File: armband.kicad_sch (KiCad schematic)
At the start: 14 parts, among them IC1 QSMP-1570, SW1 EVP-BB2A9B000, SW2 EVP-BB2A9B000

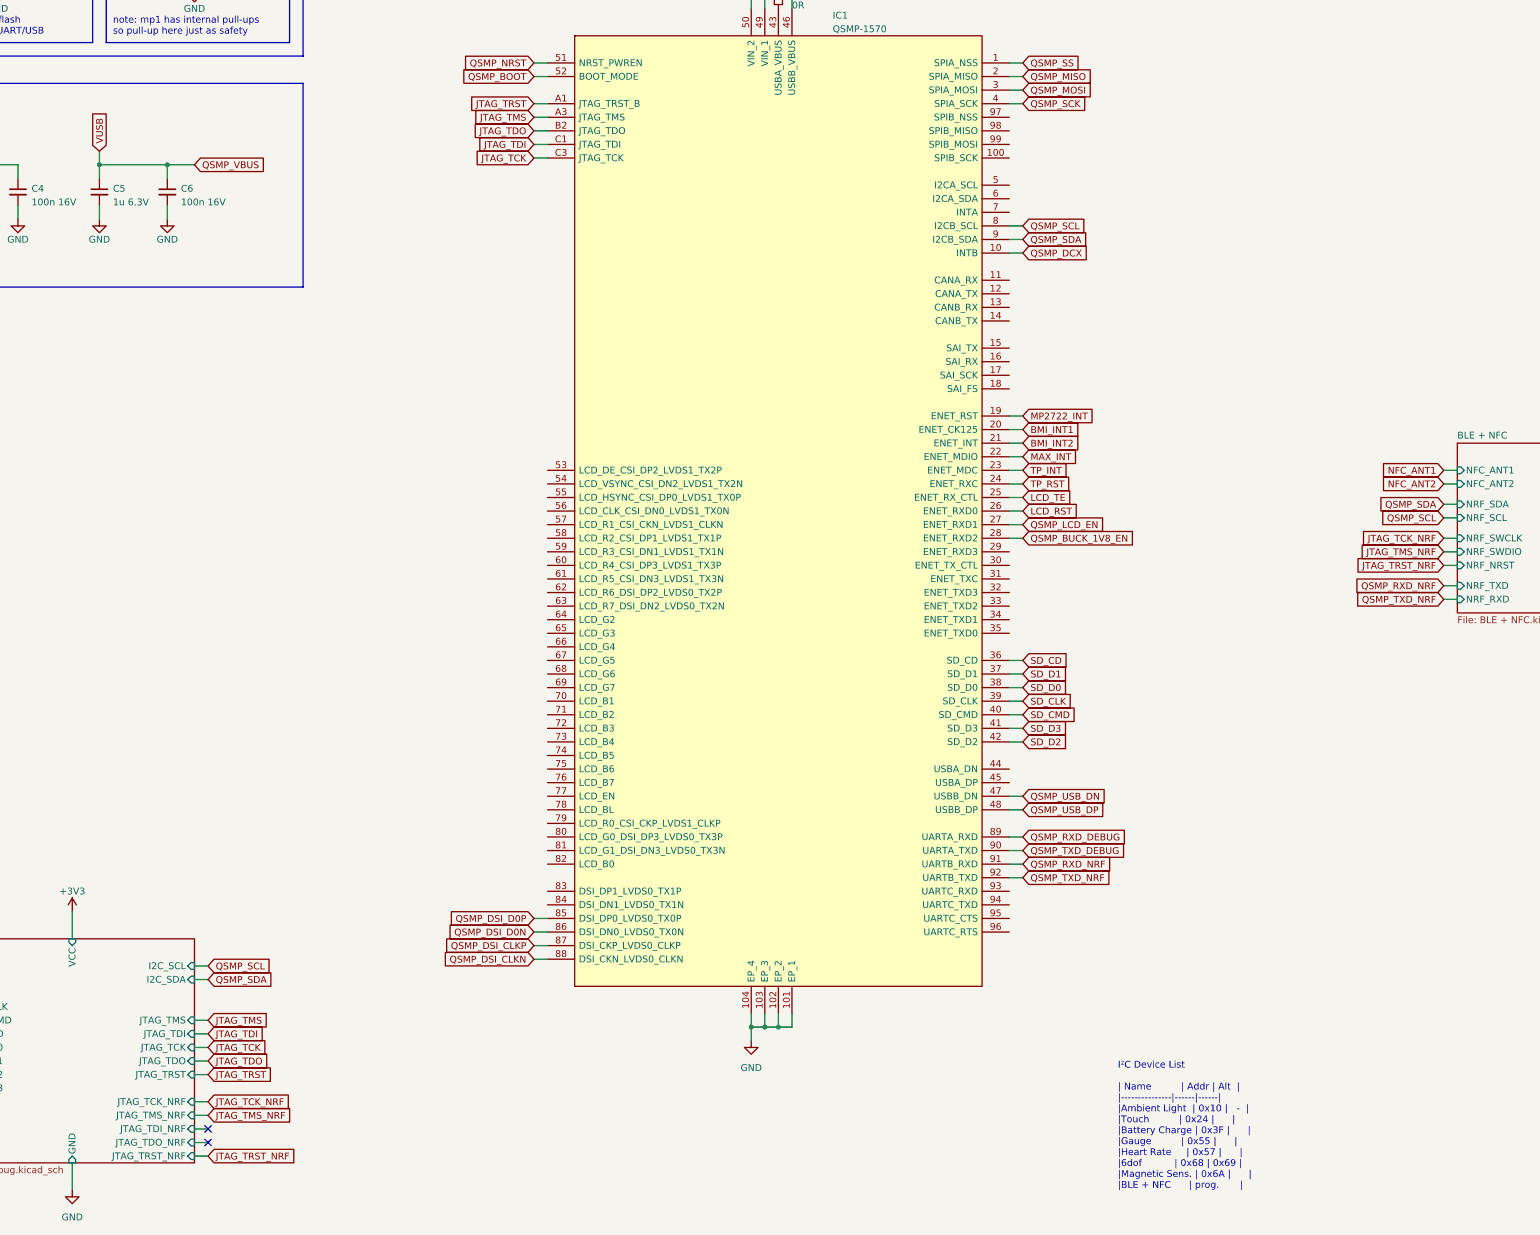
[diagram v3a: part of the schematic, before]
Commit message: updated schematic
- renamed JTAG (QSMP) and SWD (NRF) labels
- added footprint to misc. connector in debug.kicad_sch
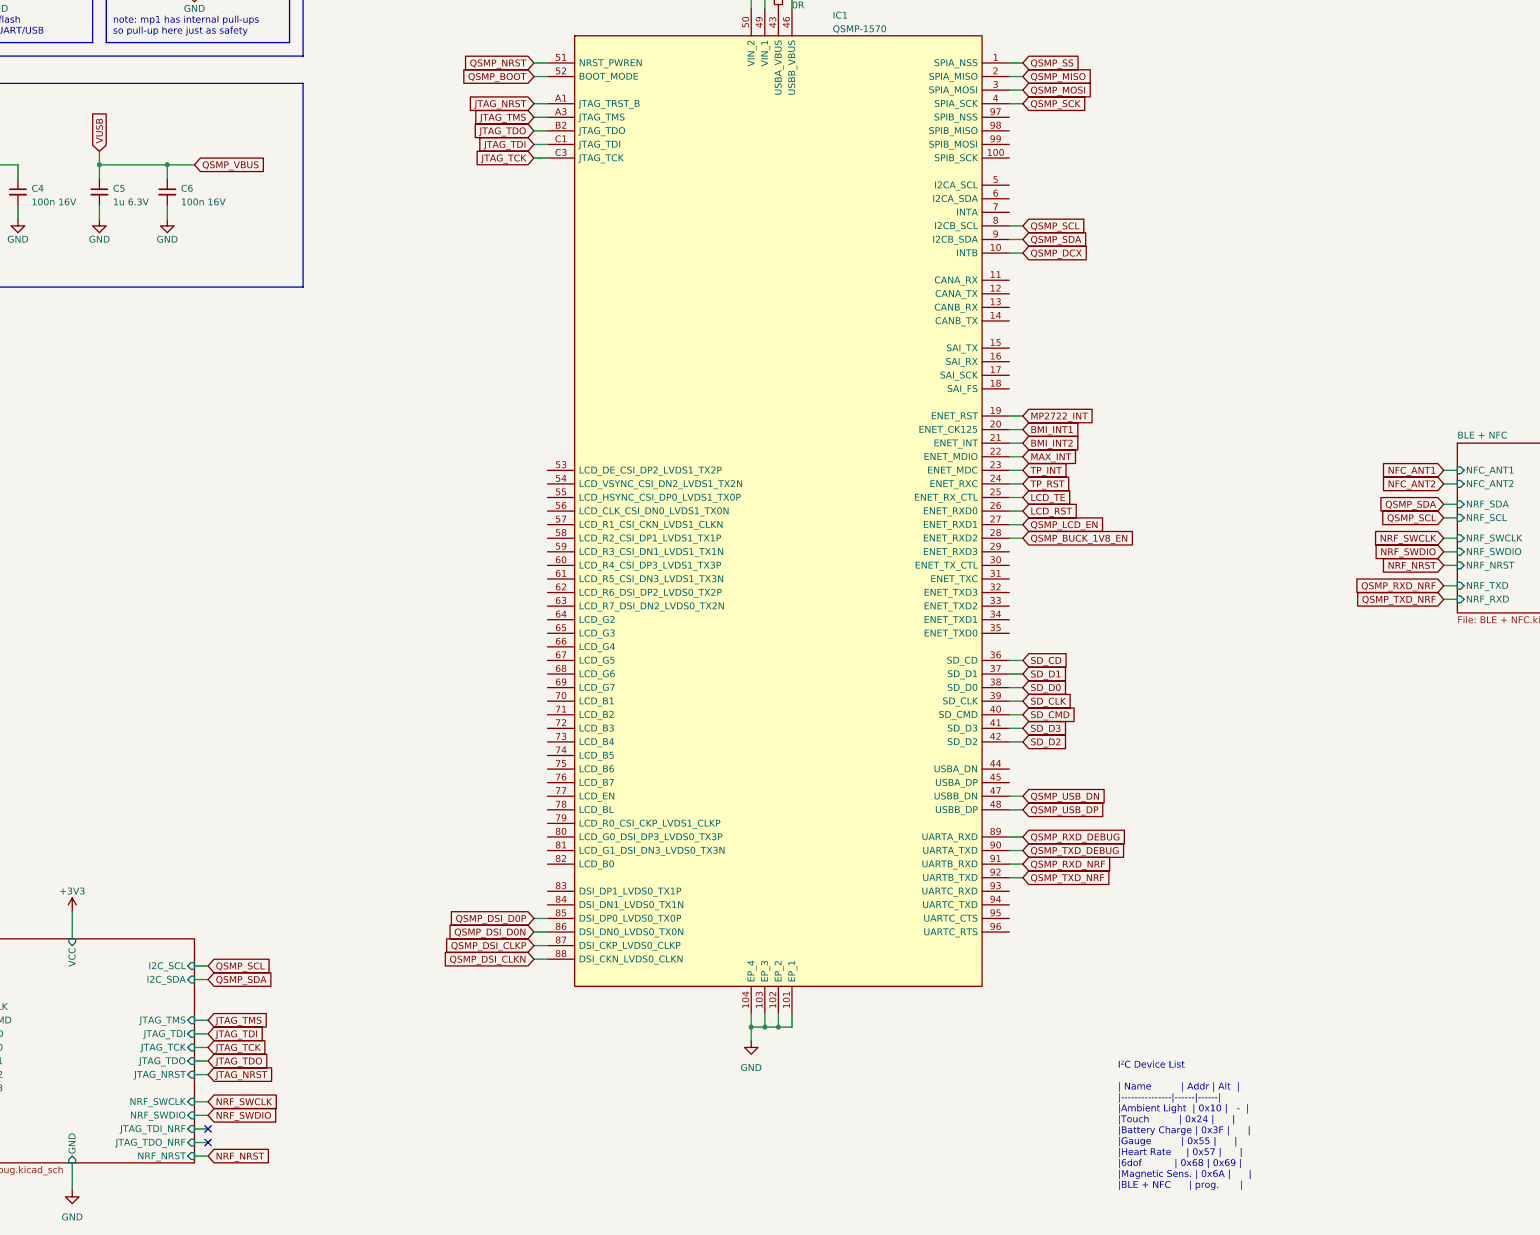
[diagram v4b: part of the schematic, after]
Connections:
- net JTAG_TRST renamed JTAG_NRST
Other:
- sheet debug ports: added JTAG_NRST, NRF_NRST, NRF_SWCLK, NRF_SWDIO; removed JTAG_TCK_NRF, JTAG_TMS_NRF, JTAG_TRST, JTAG_TRST_NRF
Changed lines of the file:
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@@
     )
   )
-  (global_label "JTAG_TMS_NRF" (shape input) (at 83.82 265.43 0) (fields_autoplaced)
+  (global_label "NRF_SWDIO" (shape input) (at 83.82 265.43 0) (fields_autoplaced)
     (effects (font (size 1.27 1.27)) (justify left))
     (property "Intersheetrefs" "${INTERSHEET_REFS}" (at 100.3518 265.43 0)
@@
     )
   )
-  (global_label "JTAG_TRST_NRF" (shape input) (at 314.96 162.56 180) (fields_autoplaced)
+  (global_label "NRF_NRST" (shape input) (at 314.96 162.56 180) (fields_autoplaced)
     (effects (font (size 1.27 1.27)) (justify right))
     (property "Intersheetrefs" "${INTERSHEET_REFS}" (at 297.642 162.56 0)
@@
     )
   )
-  (global_label "JTAG_TRST" (shape input) (at 144.78 76.2 180) (fields_autoplaced)
+  (global_label "JTAG_NRST" (shape input) (at 144.78 76.2 180) (fields_autoplaced)
     (effects (font (size 1.27 1.27)) (justify right))
     (property "Intersheetrefs" "${INTERSHEET_REFS}" (at 88.9 -25.4 0)
@@
     )
   )
-  (global_label "JTAG_TCK_NRF" (shape input) (at 314.96 157.48 180) (fields_autoplaced)
+  (global_label "NRF_SWCLK" (shape input) (at 314.96 157.48 180) (fields_autoplaced)
     (effects (font (size 1.27 1.27)) (justify right))
     (property "Intersheetrefs" "${INTERSHEET_REFS}" (at 298.5491 157.48 0)
@@
     )
   )
-  (global_label "JTAG_TMS_NRF" (shape input) (at 314.96 160.02 180) (fields_autoplaced)
+  (global_label "NRF_SWDIO" (shape input) (at 314.96 160.02 180) (fields_autoplaced)
     (effects (font (size 1.27 1.27)) (justify right))
     (property "Intersheetrefs" "${INTERSHEET_REFS}" (at 298.4282 160.02 0)
@@
     )
   )
-  (global_label "JTAG_TCK_NRF" (shape input) (at 83.82 262.89 0) (fields_autoplaced)
+  (global_label "NRF_SWCLK" (shape input) (at 83.82 262.89 0) (fields_autoplaced)
     (effects (font (size 1.27 1.27)) (justify left))
     (property "Intersheetrefs" "${INTERSHEET_REFS}" (at 100.2309 262.89 0)
@@
     )
   )
-  (global_label "JTAG_TRST_NRF" (shape input) (at 83.82 273.05 0) (fields_autoplaced)
+  (global_label "NRF_NRST" (shape input) (at 83.82 273.05 0) (fields_autoplaced)
     (effects (font (size 1.27 1.27)) (justify left))
     (property "Intersheetrefs" "${INTERSHEET_REFS}" (at 101.138 273.05 0)
@@
     )
   )
-  (global_label "JTAG_TRST" (shape input) (at 83.82 257.81 0) (fields_autoplaced)
+  (global_label "JTAG_NRST" (shape input) (at 83.82 257.81 0) (fields_autoplaced)
     (effects (font (size 1.27 1.27)) (justify left))
     (property "Intersheetrefs" "${INTERSHEET_REFS}" (at 137.16 151.13 0)
@@
       (effects (font (size 1.27 1.27)) (justify right))
     )
-    (pin "JTAG_TRST" input (at 81.28 257.81 0)
+    (pin "JTAG_NRST" input (at 81.28 257.81 0)
       (effects (font (size 1.27 1.27)) (justify right))
     )
@@
       (effects (font (size 1.27 1.27)) (justify left))
     )
-    (pin "JTAG_TCK_NRF" input (at 81.28 262.89 0)
-      (effects (font (size 1.27 1.27)) (justify right))
-    )
-    (pin "JTAG_TMS_NRF" input (at 81.28 265.43 0)
+    (pin "NRF_SWCLK" input (at 81.28 262.89 0)
+      (effects (font (size 1.27 1.27)) (justify right))
+    )
+    (pin "NRF_SWDIO" input (at 81.28 265.43 0)
       (effects (font (size 1.27 1.27)) (justify right))
     )
@@
       (effects (font (size 1.27 1.27)) (justify right))
     )
-    (pin "JTAG_TRST_NRF" input (at 81.28 273.05 0)
-      (effects (font (size 1.27 1.27)) (justify right))
-    )
+    (pin "NRF_NRST" input (at 81.28 273.05 0)
+      (effects (font (size 1.27 1.27)) (justify right))
+    )

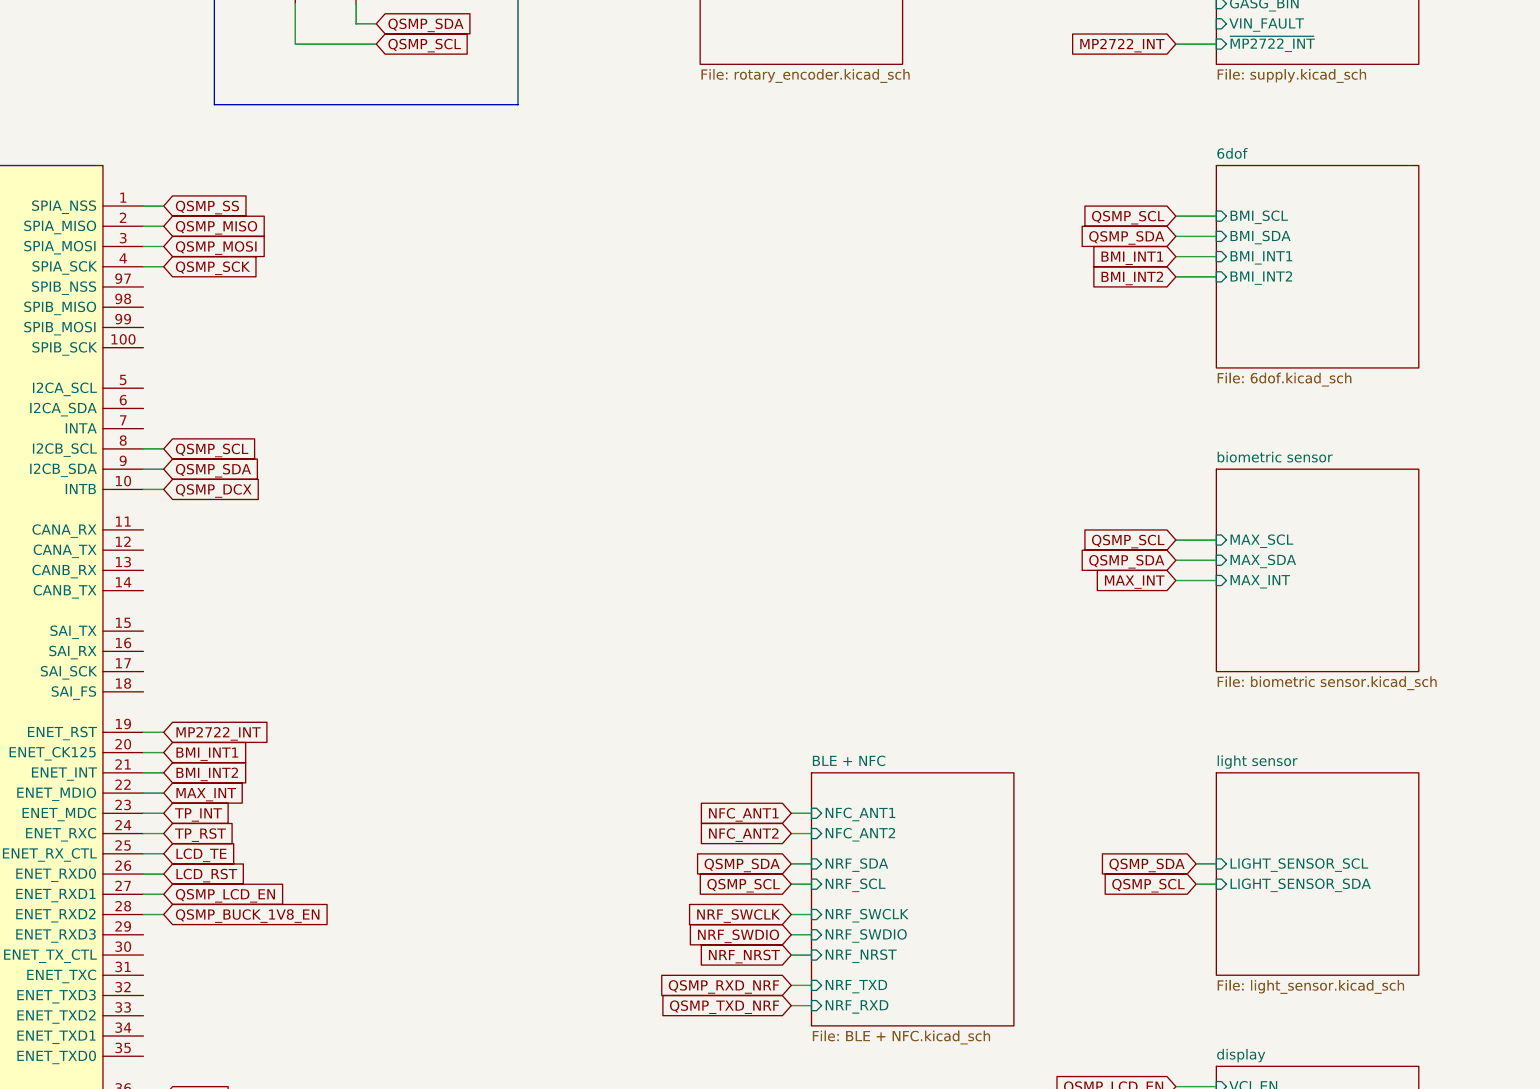
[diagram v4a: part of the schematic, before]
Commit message: added bmm350.kicad_mod and changed 9dof.kicad_sch
+ added symbol and footprint for magnetometer BMM350
+ changed supply of BMI (6dof) to 1v8
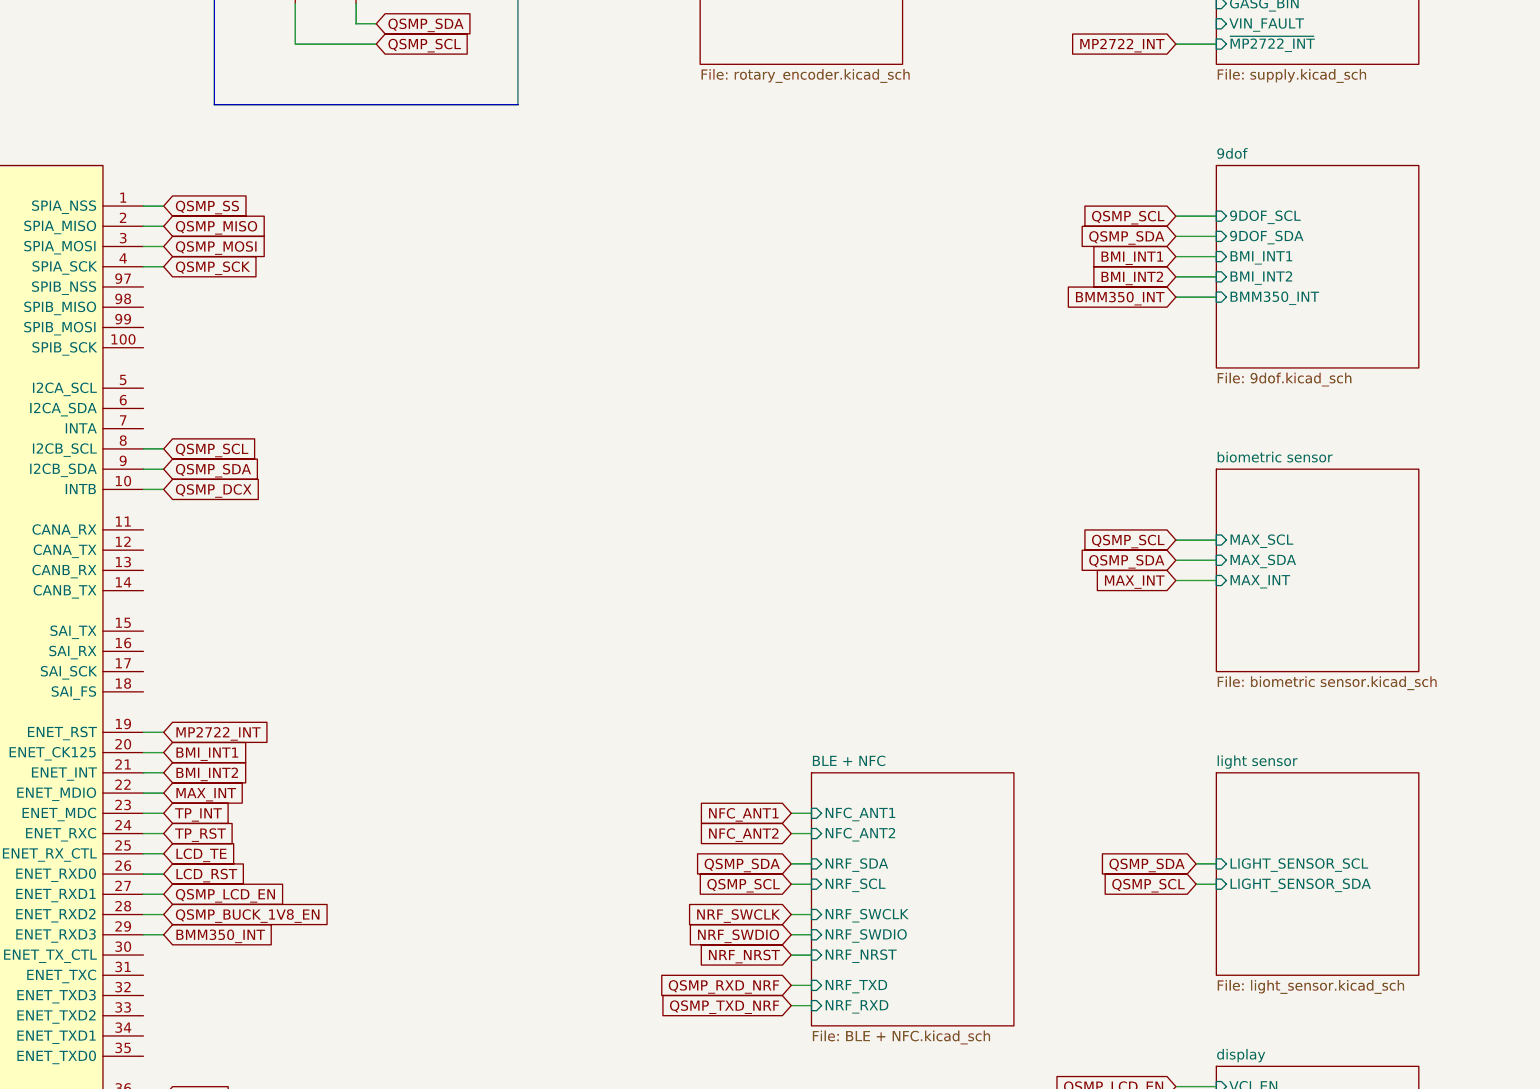
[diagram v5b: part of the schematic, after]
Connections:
- net BMM350_INT: now reaches IC1.29 (ENET_RXD3)
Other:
- sheet 6dof renamed 9dof
- sheet 9dof: file 6dof.kicad_sch -> 9dof.kicad_sch
- sheet 9dof ports: added 9DOF_SCL, 9DOF_SDA, BMM350_INT; removed BMI_SCL, BMI_SDA
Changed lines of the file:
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@@
+    (stroke (width 0) (type default))
+  )
+  (wire (pts (xy 233.68 160.02) (xy 236.22 160.02))
     (stroke (width 0) (type default))
   )
@@
   )
   (wire (pts (xy 233.68 76.2) (xy 236.22 76.2))
+    (stroke (width 0) (type default))
+  )
+  (wire (pts (xy 363.22 80.01) (xy 368.3 80.01))
     (stroke (width 0) (type default))
   )
@@
     )
   )
+  (global_label "BMM350_INT" (shape input) (at 236.22 160.02 0) (fields_autoplaced)
+    (effects (font (size 1.27 1.27)) (justify left))
+    (property "Intersheetrefs" "${INTERSHEET_REFS}" (at 250.7976 160.02 0)
+      (effects (font (size 1.27 1.27)) (justify left) hide)
+    )
+  )
   (global_label "JTAG_NRST" (shape input) (at 144.78 76.2 180) (fields_autoplaced)
     (effects (font (size 1.27 1.27)) (justify right))
@@
     (effects (font (size 1.27 1.27)) (justify right))
     (property "Intersheetrefs" "${INTERSHEET_REFS}" (at 346.2233 186.69 0)
+      (effects (font (size 1.27 1.27)) (justify right) hide)
+    )
+  )
+  (global_label "BMM350_INT" (shape input) (at 363.22 80.01 180) (fields_autoplaced)
+    (effects (font (size 1.27 1.27)) (justify right))
+    (property "Intersheetrefs" "${INTERSHEET_REFS}" (at 348.6424 80.01 0)
       (effects (font (size 1.27 1.27)) (justify right) hide)
     )
@@
     (stroke (width 0.1524) (type solid))
     (fill (color 0 0 0 0.0000))
-    (property "Sheetname" "6dof" (at 368.3 62.7884 0)
+    (property "Sheetname" "9dof" (at 368.3 62.7884 0)
       (effects (font (size 1.27 1.27)) (justify left bottom))
     )
-    (property "Sheetfile" "6dof.kicad_sch" (at 368.3 89.4846 0)
+    (property "Sheetfile" "9dof.kicad_sch" (at 368.3 89.4846 0)
       (effects (font (size 1.27 1.27)) (justify left top))
     )
-    (pin "BMI_SCL" input (at 368.3 69.85 180)
-      (effects (font (size 1.27 1.27)) (justify left))
-    )
-    (pin "BMI_SDA" input (at 368.3 72.39 180)
+    (pin "9DOF_SDA" input (at 368.3 72.39 180)
       (effects (font (size 1.27 1.27)) (justify left))
     )
@@
       (effects (font (size 1.27 1.27)) (justify left))
     )
+    (pin "9DOF_SCL" input (at 368.3 69.85 180)
+      (effects (font (size 1.27 1.27)) (justify left))
+    )
+    (pin "BMM350_INT" input (at 368.3 80.01 180)
+      (effects (font (size 1.27 1.27)) (justify left))
+    )

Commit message: Update 3d models
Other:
- note added: "I²C Device List | Name | Addr | Alt | |---------------|------|------| |Ambient Light | 0x10 | - | |BMM350 | 0x14 | 0x15 | |Touch | 0x24 | | |Battery Charge | 0x3F | | |Gauge | 0x55 | | |Heart Rate | 0x57 | | |6dof | 0x68 | 0x69 | |Magnetic Sens. | 0x6A | | |BLE + NFC | prog. |"
- note removed: "I²C Device List | Name | Addr | Alt | |---------------|------|------| |Ambient Light | 0x10 | - | |Touch | 0x24 | | |Battery Charge | 0x3F | | |Gauge | 0x55 | | |Heart Rate | 0x57 | | |6dof | 0x68 | 0x69 | |Magnetic Sens. | 0x6A | | |BLE + NFC | prog. |"
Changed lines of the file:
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@@
     (effects (font (size 1.27 1.27)) (justify left bottom))
   )
-  (text "I²C Device List\n\n| Name          | Addr | Alt  |\n|---------------|------|------|\n|Ambient Light  | 0x10 |   -  |\n|Touch          | 0x24 |      |\n|Battery Charge | 0x3F |      |  \n|Gauge          | 0x55 |      |  \n|Heart Rate     | 0x57 |      |\n|6dof           | 0x68 | 0x69 |\n|Magnetic Sens. | 0x6A |      |\n|BLE + NFC      | prog.       |"
+  (text "I²C Device List\n\n| Name          | Addr | Alt  |\n|---------------|------|------|\n|Ambient Light  | 0x10 |   -  |\n|BMM350         | 0x14 | 0x15 |\n|Touch          | 0x24 |      |\n|Battery Charge | 0x3F |      |  \n|Gauge          | 0x55 |      |  \n|Heart Rate     | 0x57 |      |\n|6dof           | 0x68 | 0x69 |\n|Magnetic Sens. | 0x6A |      |\n|BLE + NFC      | prog.       |"
     (at 254 279.4 0)
     (effects (font (face "Cascadia Mono") (size 1.27 1.27)) (justify left bottom))
